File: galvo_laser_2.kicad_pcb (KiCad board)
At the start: 2 copper layers, 33.5 x 34.2 mm, 21 parts, among them J1 Conn_01x01_Female, J2 Conn_01x01_Female, J3 Conn_01x03_Male, J4 Conn_01x03_Male, J5 AudioJack3, J6 Screw_Terminal_01x01, U1 LM324D

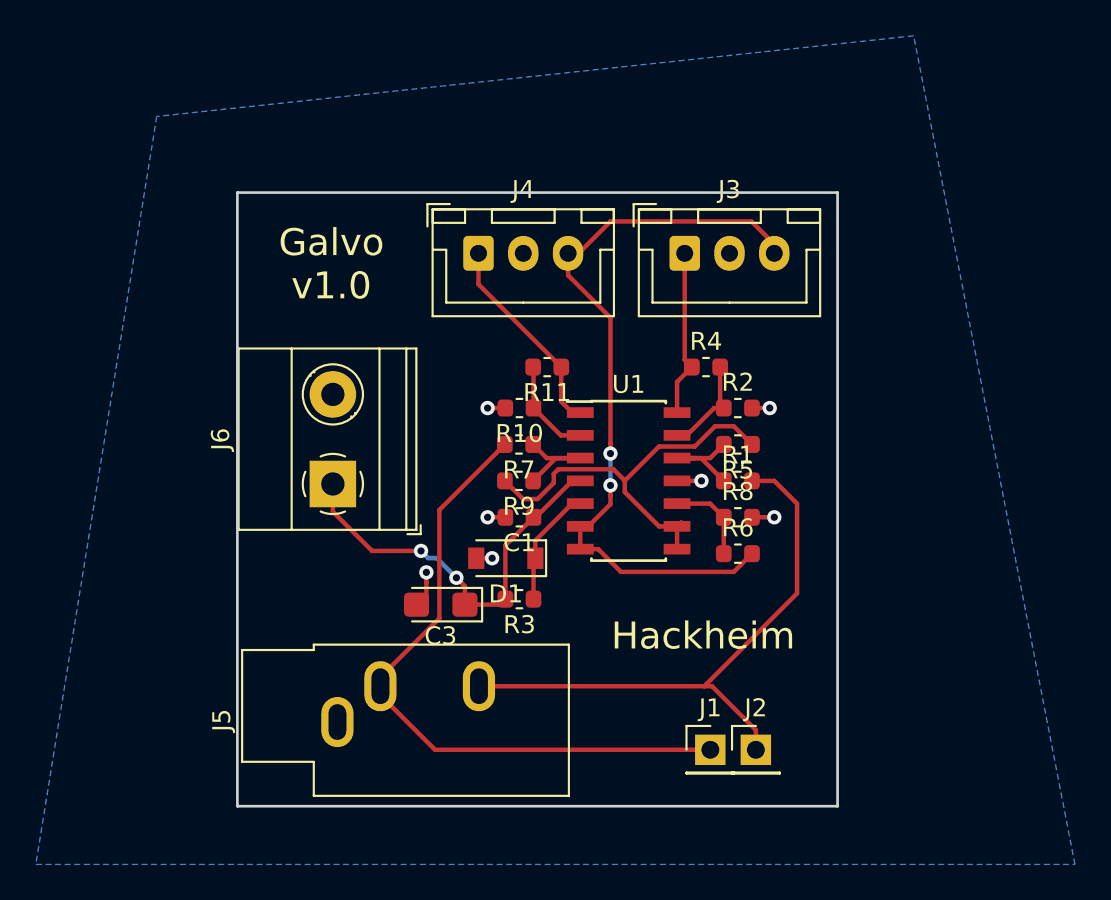
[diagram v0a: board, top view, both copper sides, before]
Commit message: Add resistor values
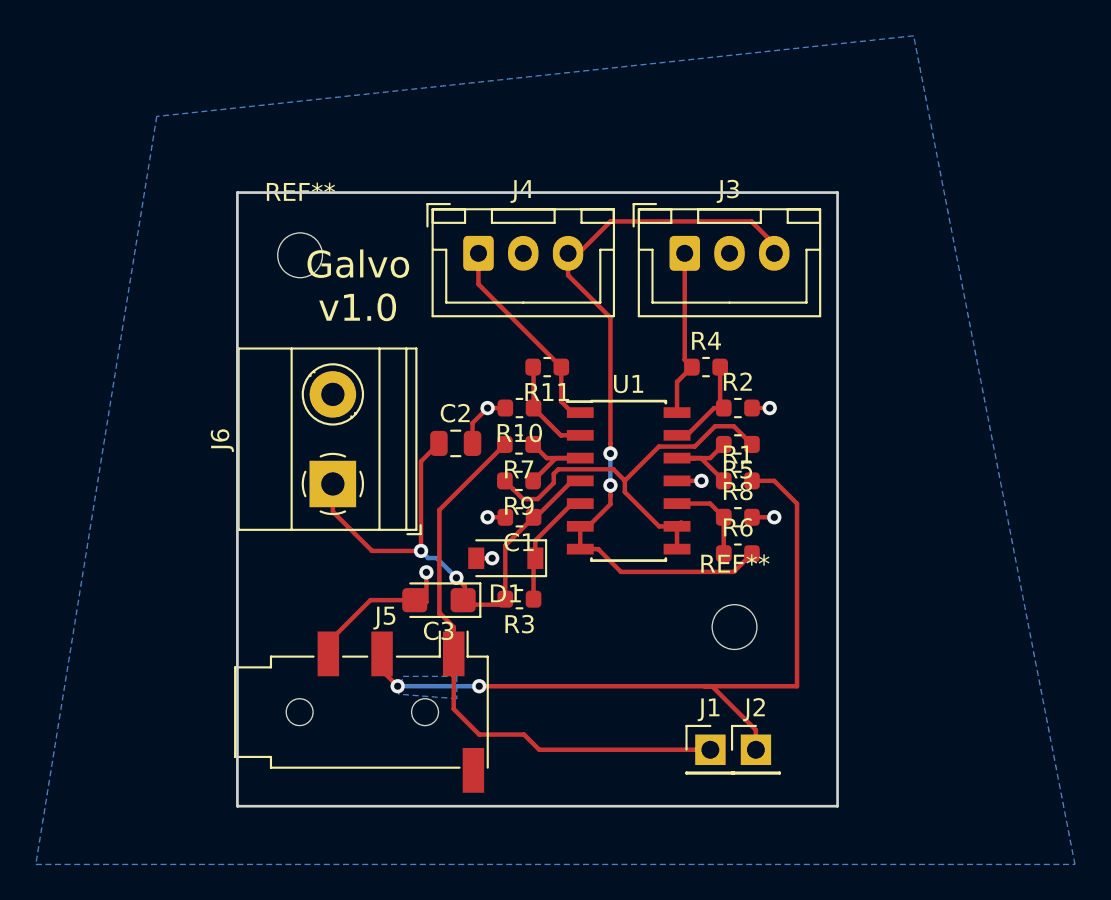
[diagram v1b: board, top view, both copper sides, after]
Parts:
- added C2: 100nF, Capacitor_SMD:C_0805_2012Metric, F.Cu at (138.9, 83.0)
- added G***: LOGO, Hackheim_logo:hackheim_logo, B.Cu at (144.5, 88.0)
- added REF**: MountingHole_2.5mm, MountingHole:MountingHole_2.5mm, F.Cu at (130.2, 72.5)
- added REF**: MountingHole_2.5mm, MountingHole:MountingHole_2.5mm, F.Cu at (154.5, 93.2)
- C1: value CP -> 1uF
- C3: value C -> 22uF
- J5: value AudioJack3 -> AudioJack4; footprint Connector_Audio:Jack_3.5mm_CUI_SJ1-3533NG_Horizontal -> Connector_Audio:Jack_3.5mm_PJ320D_Horizontal
- moved J5 2.72 mm to (135.0, 98.0), turned to 0 degrees
- moved C3 0.27 mm to (138.0, 91.8)
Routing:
- net Net-(J2-Pad1): track 32.9 -> 42.7 mm, vias 0 -> 2
- net GND: track 8.33 -> 17.1 mm
- net VCC: track 22.7 -> 29.1 mm
- net Net-(J1-Pad1): track 36.6 -> 31.9 mm
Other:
- board text removed: "Hackheim"

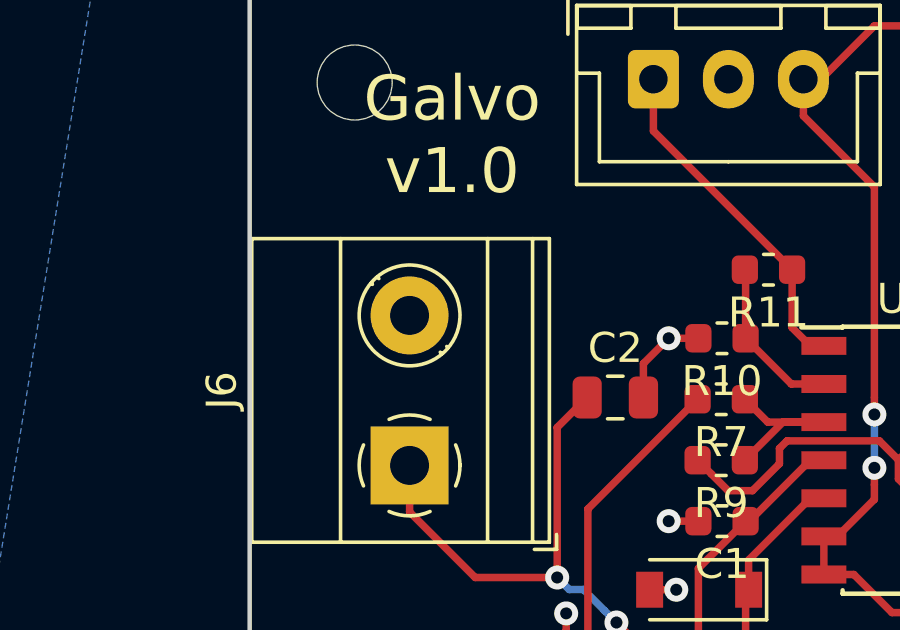
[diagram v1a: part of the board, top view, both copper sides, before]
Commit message: Connect screw terminal to ground
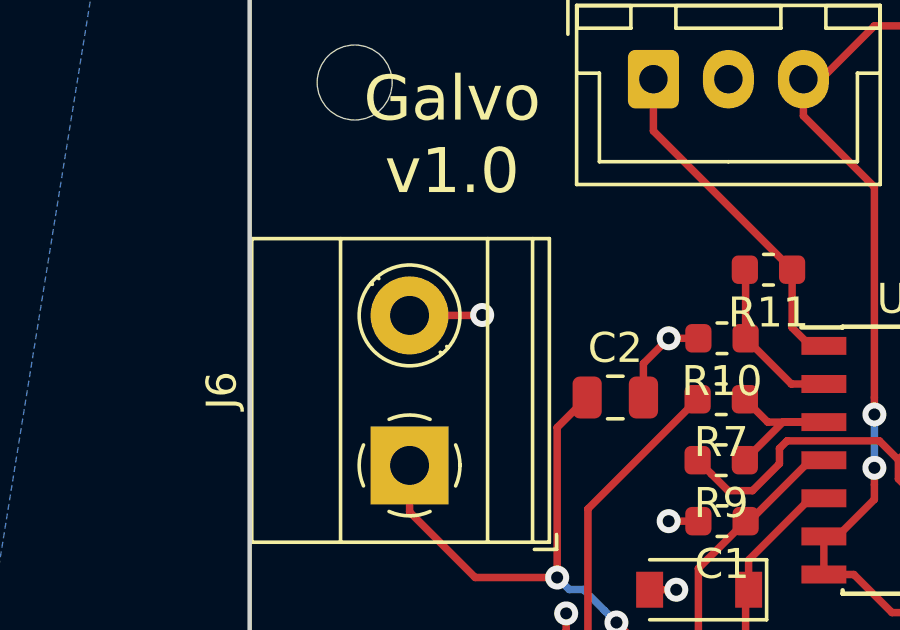
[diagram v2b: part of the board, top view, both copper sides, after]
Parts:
- J6: value Screw_Terminal_01x01 -> Screw_Terminal_01x02
- R1, R10, R2, R7: value R -> 2.7k
- R11, R3, R4, R5, R6, R9: value R -> 10k
- R8: value R -> 1.8k
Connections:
- J6 pad 2: (no net) -> GND
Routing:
- net GND: track 17.1 -> 19.5 mm, vias 7 -> 8
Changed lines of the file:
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@@
     (thickness 1.6)
     (drawings 5)
-    (tracks 142)
+    (tracks 145)
     (zones 0)
     (modules 25)
@@
       (effects (font (size 1 1) (thickness 0.15)))
     )
-    (fp_text value R (at 0 1.43) (layer F.Fab)
+    (fp_text value 2.7k (at 0 1.43) (layer F.Fab)
       (effects (font (size 1 1) (thickness 0.15)))
     )
@@
       (effects (font (size 1 1) (thickness 0.15)))
     )
-    (fp_text value R (at 0 1.43) (layer F.Fab)
+    (fp_text value 2.7k (at 0 1.43) (layer F.Fab)
       (effects (font (size 1 1) (thickness 0.15)))
     )
@@
       (effects (font (size 1 1) (thickness 0.15)))
     )
-    (fp_text value R (at 0 1.43 180) (layer F.Fab)
+    (fp_text value 10k (at 0 1.43 180) (layer F.Fab)
       (effects (font (size 1 1) (thickness 0.15)))
     )
@@
       (effects (font (size 1 1) (thickness 0.15)))
     )
-    (fp_text value R (at 0 1.43) (layer F.Fab)
+    (fp_text value 10k (at 0 1.43) (layer F.Fab)
       (effects (font (size 1 1) (thickness 0.15)))
     )
@@
       (effects (font (size 1 1) (thickness 0.15)))
     )
-    (fp_text value R (at 0 1.43 180) (layer F.Fab)
+    (fp_text value 10k (at 0 1.43 180) (layer F.Fab)
       (effects (font (size 1 1) (thickness 0.15)))
     )
@@
       (effects (font (size 1 1) (thickness 0.15)))
     )
-    (fp_text value R (at 0 1.43) (layer F.Fab)
+    (fp_text value 10k (at 0 1.43) (layer F.Fab)
       (effects (font (size 1 1) (thickness 0.15)))
     )
@@
       (effects (font (size 1 1) (thickness 0.15)))
     )
-    (fp_text value R (at 0 1.43 180) (layer F.Fab)
+    (fp_text value 2.7k (at 0 1.43 180) (layer F.Fab)
       (effects (font (size 1 1) (thickness 0.15)))
     )
@@
       (effects (font (size 1 1) (thickness 0.15)))
     )
-    (fp_text value R (at 0 1.43) (layer F.Fab)
+    (fp_text value 1.8k (at 0 1.43) (layer F.Fab)
       (effects (font (size 1 1) (thickness 0.15)))
     )
@@
       (effects (font (size 1 1) (thickness 0.15)))
     )
-    (fp_text value R (at 0 1.43 180) (layer F.Fab)
+    (fp_text value 10k (at 0 1.43 180) (layer F.Fab)
       (effects (font (size 1 1) (thickness 0.15)))
     )
@@
       (effects (font (size 1 1) (thickness 0.15)))
     )
-    (fp_text value R (at 0 1.43 180) (layer F.Fab)
+    (fp_text value 2.7k (at 0 1.43 180) (layer F.Fab)
       (effects (font (size 1 1) (thickness 0.15)))
     )
@@
       (effects (font (size 1 1) (thickness 0.15)))
     )
-    (fp_text value R (at 0 1.43 180) (layer F.Fab)
+    (fp_text value 10k (at 0 1.43 180) (layer F.Fab)
       (effects (font (size 1 1) (thickness 0.15)))
     )
@@
       (effects (font (size 1 1) (thickness 0.15)))
     )
-    (fp_text value Screw_Terminal_01x01 (at 2.5 5.66 90) (layer F.Fab)
+    (fp_text value Screw_Terminal_01x02 (at 2.5 5.66 90) (layer F.Fab)
       (effects (font (size 1 1) (thickness 0.15)))
     )
@@
     (pad 1 thru_hole rect (at 0 0 90) (size 2.6 2.6) (drill 1.3) (layers *.Cu *.Mask)
       (net 10 VCC))
-    (pad 2 thru_hole circle (at 5 0 90) (size 2.6 2.6) (drill 1.3) (layers *.Cu *.Mask))
+    (pad 2 thru_hole circle (at 5 0 90) (size 2.6 2.6) (drill 1.3) (layers *.Cu *.Mask)
+      (net 2 GND))
     (model ${KISYS3DMOD}/TerminalBlock_Phoenix.3dshapes/TerminalBlock_Phoenix_MKDS-1,5-2_1x02_P5.00mm_Horizontal.wrl
       (at (xyz 0 0 0))
@@
   (segment (start 139.875 81.867) (end 140.716 81.026) (width 0.25) (layer F.Cu) (net 2))
   (segment (start 139.875 83) (end 139.875 81.867) (width 0.25) (layer F.Cu) (net 2))
+  (via (at 134.5 80.25) (size 0.8) (drill 0.4) (layers F.Cu B.Cu) (net 2))
+  (segment (start 132.08 80.264) (end 134.486 80.264) (width 0.25) (layer F.Cu) (net 2))
+  (segment (start 134.486 80.264) (end 134.5 80.25) (width 0.25) (layer F.Cu) (net 2))
   (segment (start 143.6 100.1) (end 153.15 100.1) (width 0.25) (layer F.Cu) (net 3))
   (segment (start 142.75 99.25) (end 143.6 100.1) (width 0.25) (layer F.Cu) (net 3))

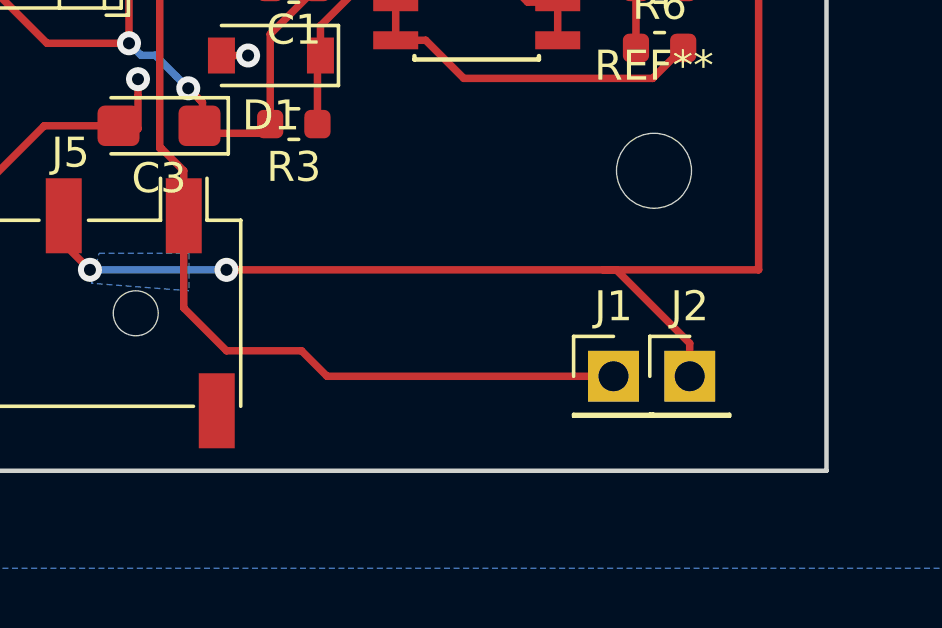
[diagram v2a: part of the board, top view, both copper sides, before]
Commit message: Add ground connector for microcontroller
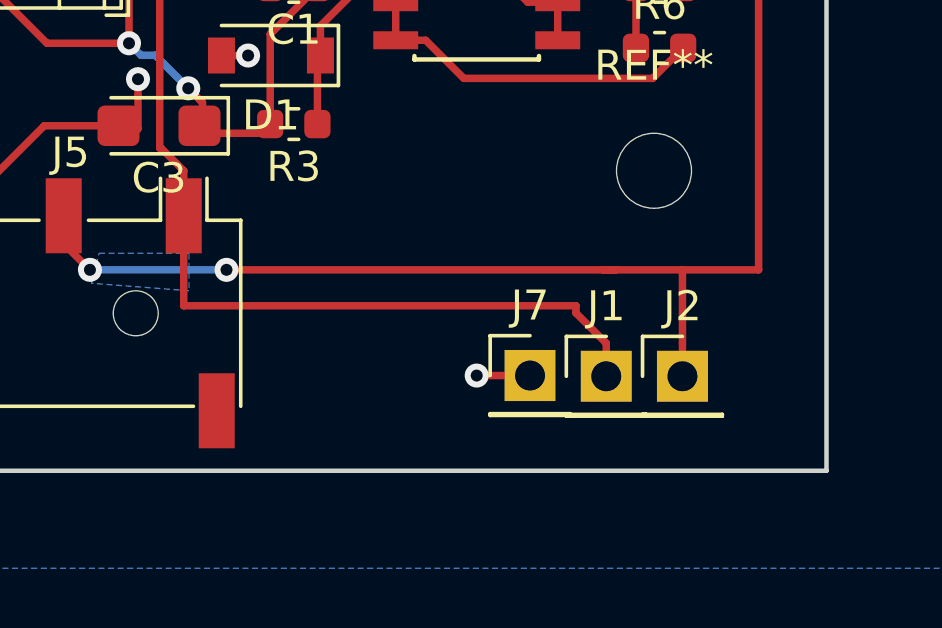
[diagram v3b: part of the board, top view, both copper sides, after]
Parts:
- removed G***: LOGO, Hackheim_logo:hackheim_logo
- added J7: Conn_01x01_Female, Connector_PinHeader_2.54mm:PinHeader_1x01_P2.54mm_Vertical, F.Cu at (150.4, 100.1)
- moved J1 0.24 mm to (152.9, 100.1)
- moved J2 0.24 mm to (155.4, 100.1)
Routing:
- net GND: track 19.5 -> 21.3 mm, vias 8 -> 9
- net Net-(J2-Pad1): track 42.7 -> 41.7 mm
- net Net-(J1-Pad1): track 31.9 -> 32.4 mm
